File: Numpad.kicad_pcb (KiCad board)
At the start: 2 copper layers, 76.2 x 97.6 mm, 51 parts, among them J1 USB_B_Mini, SW0 0, SW1 1, SW2 2, SW3 3, SW4 4, SW5 5, SW6 6, SW7 7, SW8 8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

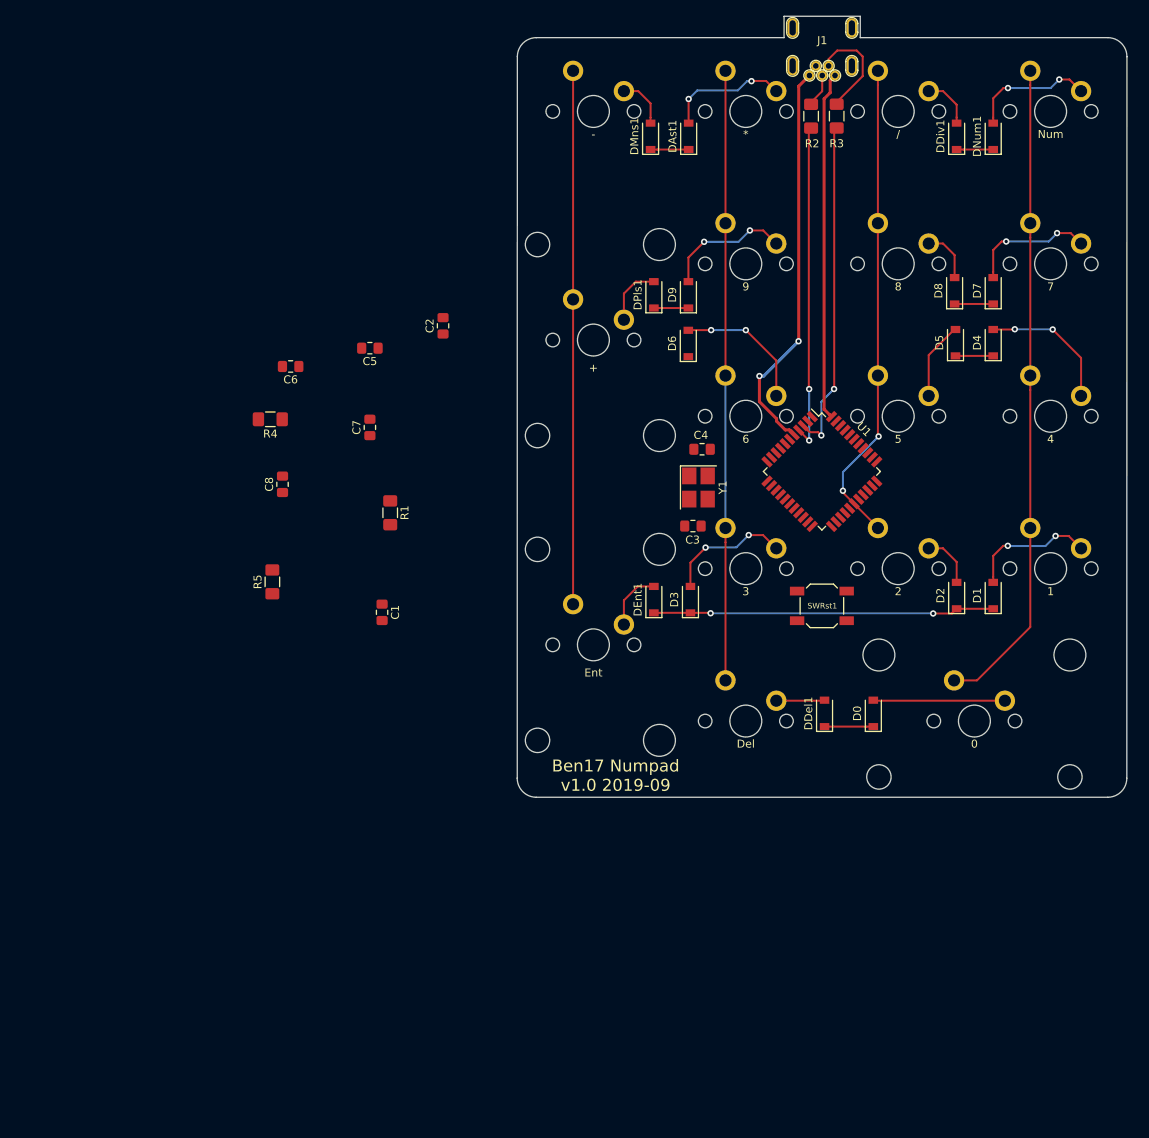
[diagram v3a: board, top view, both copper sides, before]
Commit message: allowed split + key
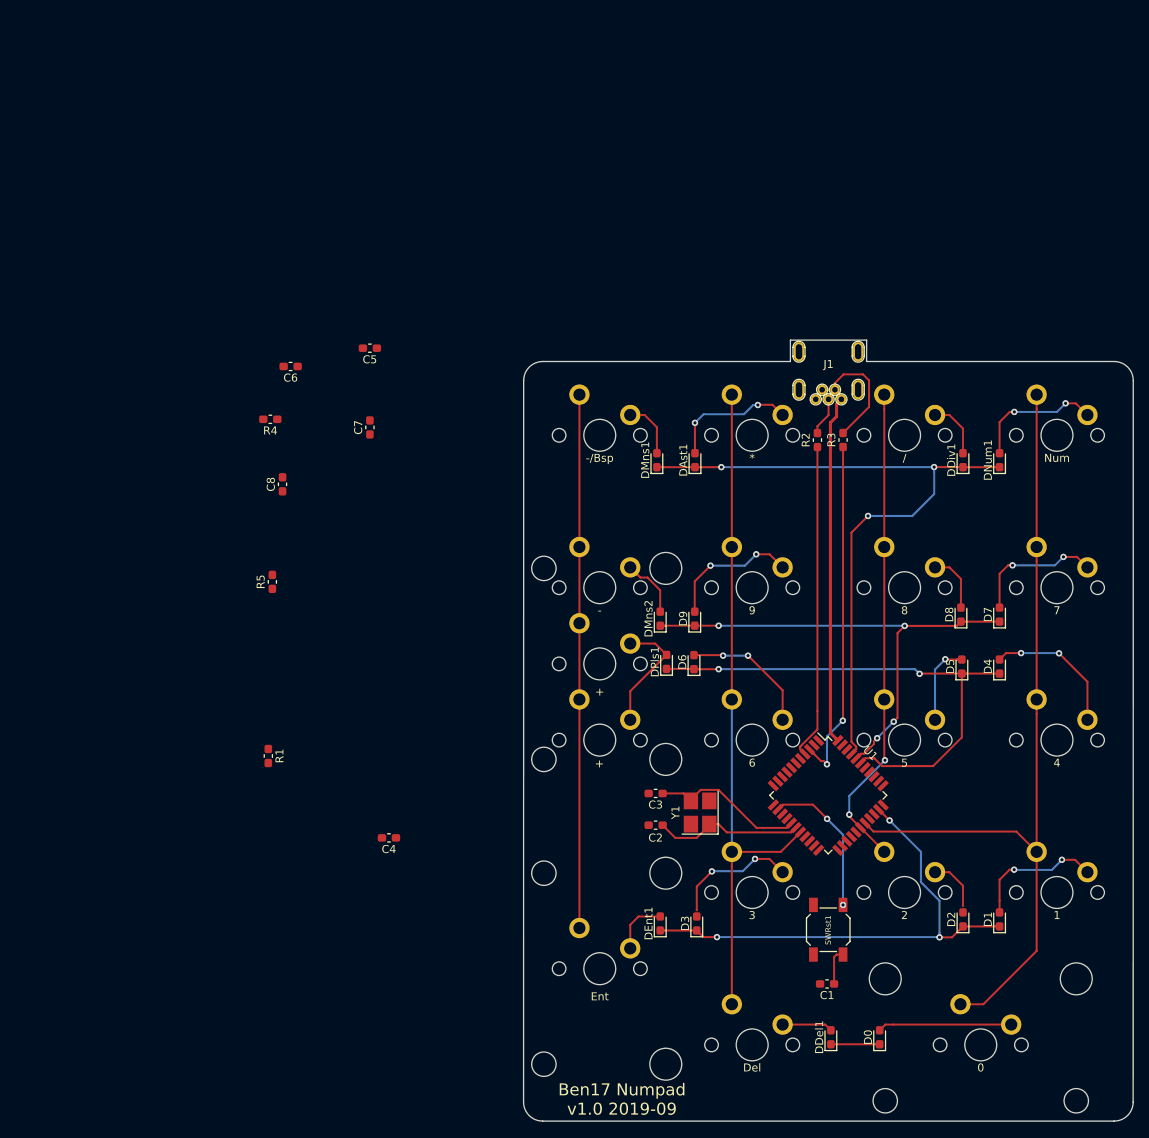
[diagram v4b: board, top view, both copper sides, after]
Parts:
- added DPls1: 1N4148W, Diode_SMD:D_0603_1608Metric_Pad1.05x0.95mm_HandSolder, F.Cu at (176.8, 117.7)
- added SWMns2: -, AcheronMX:MX100, F.Cu at (168.4, 108.4)
- added SWPls2: +, AcheronMX:MX100, F.Cu at (168.4, 127.5)
- C1: value 22pF -> 100nF; footprint Capacitor_SMD:C_0805_2012Metric_Pad1.15x1.40mm_HandSolder -> Capacitor_SMD:C_0603_1608Metric_Pad1.05x0.95mm_HandSolder
- C2, C3, C4, C5, C6, C7, C8: footprint Capacitor_SMD:C_0805_2012Metric_Pad1.15x1.40mm_HandSolder -> Capacitor_SMD:C_0603_1608Metric_Pad1.05x0.95mm_HandSolder
- D0, D1, D2, D3, D4, D5, D6, D7, D8, D9, DAst1, DDel1, DDiv1, DEnt1, DMns1, DNum1: footprint Diode_SMD:D_SOD-123 -> Diode_SMD:D_0603_1608Metric_Pad1.05x0.95mm_HandSolder
- DMns2: renamed from DPls1; footprint Diode_SMD:D_SOD-123 -> Diode_SMD:D_0603_1608Metric_Pad1.05x0.95mm_HandSolder
- R1, R2, R3, R4, R5: footprint Resistor_SMD:R_1206_3216Metric_Pad1.42x1.75mm_HandSolder -> Resistor_SMD:R_0603_1608Metric_Pad1.05x0.95mm_HandSolder
- SWMns1: value - -> -/Bsp
- moved C1 72.5 mm to (196.8, 158.0), turned to 180 degrees
- moved C2 67.8 mm to (175.4, 138.1), turned to 0 degrees
- moved C4 62.4 mm to (142.1, 139.7)
- moved Y1 40.6 mm to (181.0, 136.5), turned to 90 degrees
- moved D3 40.5 mm to (180.6, 150.4)
- moved DEnt1 40.5 mm to (176.0, 150.4)
- moved SWEnt1 40.5 mm to (168.4, 156.1)
- moved R3 40.5 mm to (198.8, 90.0)
- moved D0 40.5 mm to (203.4, 164.6)
- moved D1 40.5 mm to (218.4, 149.9)
- moved D2 40.5 mm to (213.8, 149.9)
- moved D4 40.5 mm to (218.4, 118.3)
- moved D5 40.5 mm to (213.7, 118.3)
- moved D9 40.5 mm to (180.3, 112.3)
- moved DAst1 40.5 mm to (180.3, 92.5)
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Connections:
- C1 pad 2: Net-(C1-Pad2) -> GND
- DMns2 pad 2: Net-(DPls1-Pad2) -> Net-(DMns2-Pad2)
- R5 pad 1: Net-(C1-Pad2) -> Net-(R5-Pad1)
- SWRst1 pad 2: Net-(C1-Pad2) -> Net-(R5-Pad1)
- U1 pad 18: Net-(U1-Pad18) -> Col3
- U1 pad 26: Col3 -> Net-(U1-Pad26)
- U1 pad 32: Net-(U1-Pad32) -> Row4
- U1 pad 38: Row4 -> Net-(U1-Pad38)
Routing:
- net Row1: track 9.33 -> 86.7 mm, vias 0 -> 3
- net Row3: track 4.78 -> 64.8 mm, vias 0 -> 2
- net Row2: track 9.14 -> 62.0 mm, vias 0 -> 4
- net GND: track 49.9 -> 0.00 mm, vias 2 -> 0
- net RST: track 0.00 -> 23.3 mm, vias 0 -> 2
- net Col1: track 81.8 -> 104.8 mm
- net Row4: track 42.7 -> 62.5 mm, vias 2 -> 3
- net Net-(C3-Pad1): track 0.00 -> 19.4 mm
- net Net-(C2-Pad2): track 0.00 -> 18.8 mm
- net Col3: track 76.2 -> 85.8 mm
- net Net-(DMns2-Pad2): track 0.00 -> 7.61 mm
- net Net-(DPls1-Pad2): track 7.63 -> 15.1 mm
- net D-: track 41.8 -> 43.4 mm
- net D+: track 40.9 -> 39.5 mm, vias 2 -> 0
- net Net-(D5-Pad2): track 9.78 -> 10.8 mm, vias 0 -> 1
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
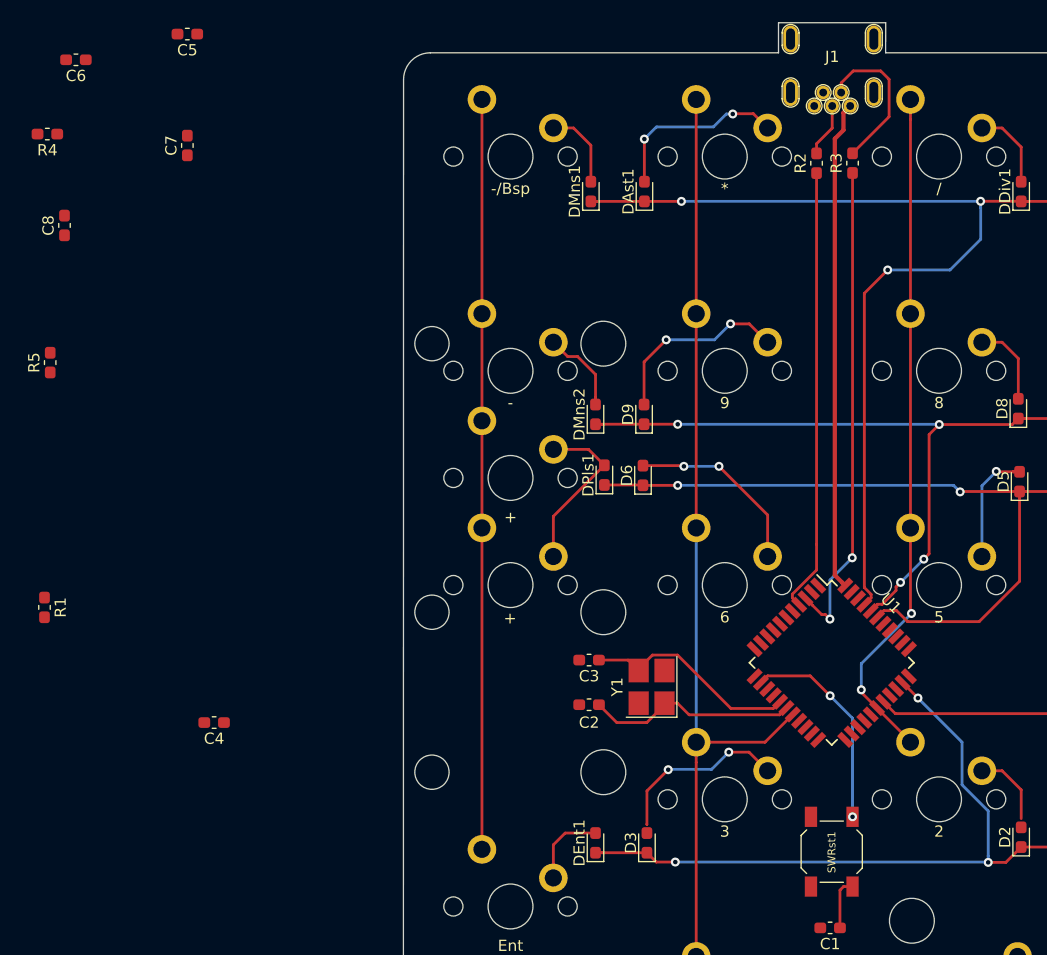
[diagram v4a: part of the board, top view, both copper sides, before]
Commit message: all componentes withing the confines of the board now, still need to add ground. Not shure about the components around reset button or c5 & c9's grounding
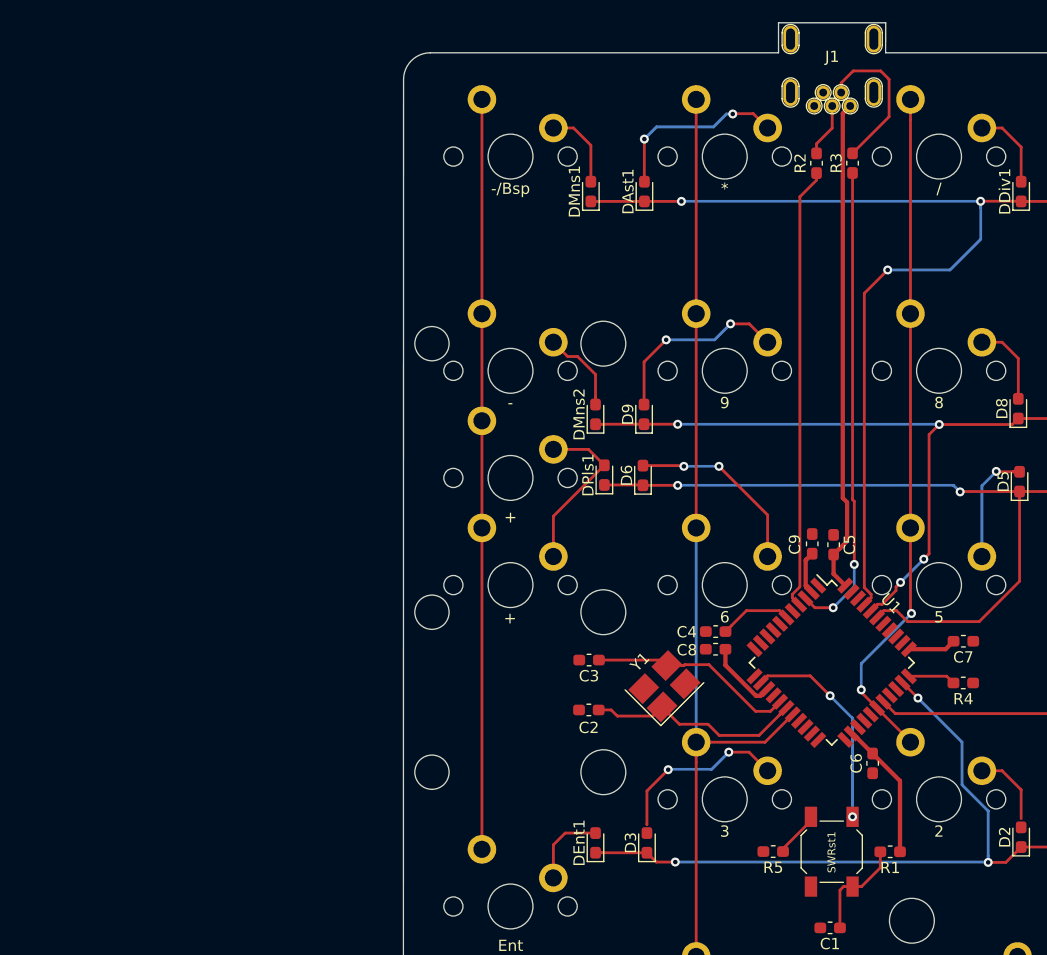
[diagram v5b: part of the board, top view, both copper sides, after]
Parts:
- added C9: 0.1uF, Capacitor_SMD:C_0603_1608Metric_Pad1.05x0.95mm_HandSolder, F.Cu at (195.3, 123.8)
- C5: value 10uF -> 4.7uF
- C6: value 1uF -> 0.1uF
- C8: value 01.uF -> 0.1uF
- moved R4 94.9 mm to (208.7, 136.2)
- moved C6 94.5 mm to (200.6, 143.3), turned to 90 degrees
- moved C7 81.9 mm to (208.7, 132.5), turned to 180 degrees
- moved R1 78.3 mm to (202.2, 151.2), turned to 180 degrees
- moved R5 77.6 mm to (191.8, 151.2), turned to 180 degrees
- moved C5 73.2 mm to (197.2, 123.9), turned to 270 degrees
- moved C8 69.1 mm to (186.7, 133.2), turned to 0 degrees
- moved C4 45.3 mm to (186.7, 131.6)
- moved Y1 1.15 mm to (182.1, 136.5), turned to 45 degrees
- moved C2 0.47 mm to (175.4, 138.6)
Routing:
- net +5V: track 43.6 -> 71.1 mm
- net Net-(C4-Pad1): track 0.00 -> 6.43 mm
- net RST: track 23.3 -> 27.9 mm
- net Net-(R4-Pad2): track 0.00 -> 4.21 mm
- net Net-(R5-Pad1): track 0.00 -> 4.12 mm
- net Net-(C2-Pad2): track 18.8 -> 20.2 mm
- net D-: track 43.4 -> 42.3 mm
- net Net-(C3-Pad1): track 19.4 -> 18.4 mm

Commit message: we can now have a maxiumum of 18 keys, so renamed it Ben18 from Ben17
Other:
- board text added: "Ben18 Numpad v1.0 2019-10"
- board text removed: "Ben17 Numpad v1.0 2019-09"
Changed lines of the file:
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@@
   (gr_line (start 201.79375 77.48125) (end 201.78625 80.15125) (layer Edge.Cuts) (width 0.05))
   (gr_line (start 192.26125 80.15125) (end 192.26125 77.48125) (layer Edge.Cuts) (width 0.05))
-  (gr_text "Ben17 Numpad\nv1.0 2019-09" (at 171.21505 172.39615) (layer F.SilkS)
+  (gr_text "Ben18 Numpad\nv1.0 2019-10" (at 171.21505 172.39615) (layer F.SilkS)
     (effects (font (size 1.5 1.5) (thickness 0.3)))
   )

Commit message: ground planes in, thinking about ordering
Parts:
- D0, D1, D2, D3, D4, D5, D6, D7, D8, D9, DAst1, DDel1, DDiv1, DEnt1, DMns1, DMns2, DNum1, DPls1: footprint Diode_SMD:D_0603_1608Metric_Pad1.05x0.95mm_HandSolder -> Diode_SMD:D_SOD-323_HandSoldering
- J1: footprint AcheronConnectors:USB_MiniB_XM7D-0512 -> digikey-kicad-library:USB_Mini_B_Female_548190519
- moved C9 56.9 mm to (146.0, 95.3)
- moved C4 56.5 mm to (137.6, 103.7)
- moved C8 56.5 mm to (137.6, 105.3)
- moved C5 56.4 mm to (148.4, 95.4)
- moved R3 56.4 mm to (148.1, 65.4)
- moved D6 56.2 mm to (131.4, 90.0)
- moved C1 56.2 mm to (148.0, 130.2)
- moved C2 56.2 mm to (126.6, 110.8)
- moved C6 56.2 mm to (151.8, 115.6)
- moved D3 56.2 mm to (131.7, 122.7)
- moved DEnt1 56.2 mm to (127.2, 122.7)
- moved SWEnt1 56.2 mm to (119.6, 128.3)
- moved D1 56.2 mm to (169.6, 122.2)
- moved D2 56.2 mm to (165.0, 122.2)
- moved D4 56.2 mm to (169.6, 90.6)
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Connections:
- R2 pad 1: D+ -> D-
- R2 pad 2: Net-(J1-Pad3) -> Net-(J1-Pad2)
- R3 pad 1: D- -> D+
- R3 pad 2: Net-(J1-Pad2) -> Net-(J1-Pad3)
- U1 pad 19: Net-(U1-Pad19) -> Col4
- U1 pad 25: Col4 -> Net-(U1-Pad25)
- U1 pad 26: Net-(U1-Pad26) -> Row5
- U1 pad 37: Row5 -> Net-(U1-Pad37)
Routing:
- net Col4: track 66.7 -> 99.6 mm, vias 0 -> 1
- net GND: track 0.00 -> 31.1 mm, vias 0 -> 4
- net +5V: track 71.1 -> 99.3 mm
- net Row5: track 6.10 -> 33.6 mm
- net Net-(J1-Pad2): track 13.8 -> 5.80 mm
- net RST: track 27.9 -> 35.6 mm
- net Net-(R5-Pad1): track 4.12 -> 8.25 mm
- net Net-(DDel1-Pad2): track 6.33 -> 8.12 mm
- net Net-(J1-Pad3): track 4.79 -> 3.12 mm
- net Net-(D3-Pad2): track 15.8 -> 14.5 mm
- net Net-(DEnt1-Pad2): track 7.12 -> 5.99 mm
- net D-: track 42.3 -> 41.4 mm
- net Net-(D0-Pad2): track 16.7 -> 17.6 mm
- net Row2: track 62.0 -> 61.2 mm
- net Net-(D1-Pad2): track 16.8 -> 16.1 mm
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- added copper zone on B.Cu, net GND
- added copper zone on F.Cu, net GND
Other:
- board size 76.2 x 97.6 mm -> 76.2 x 95 mm

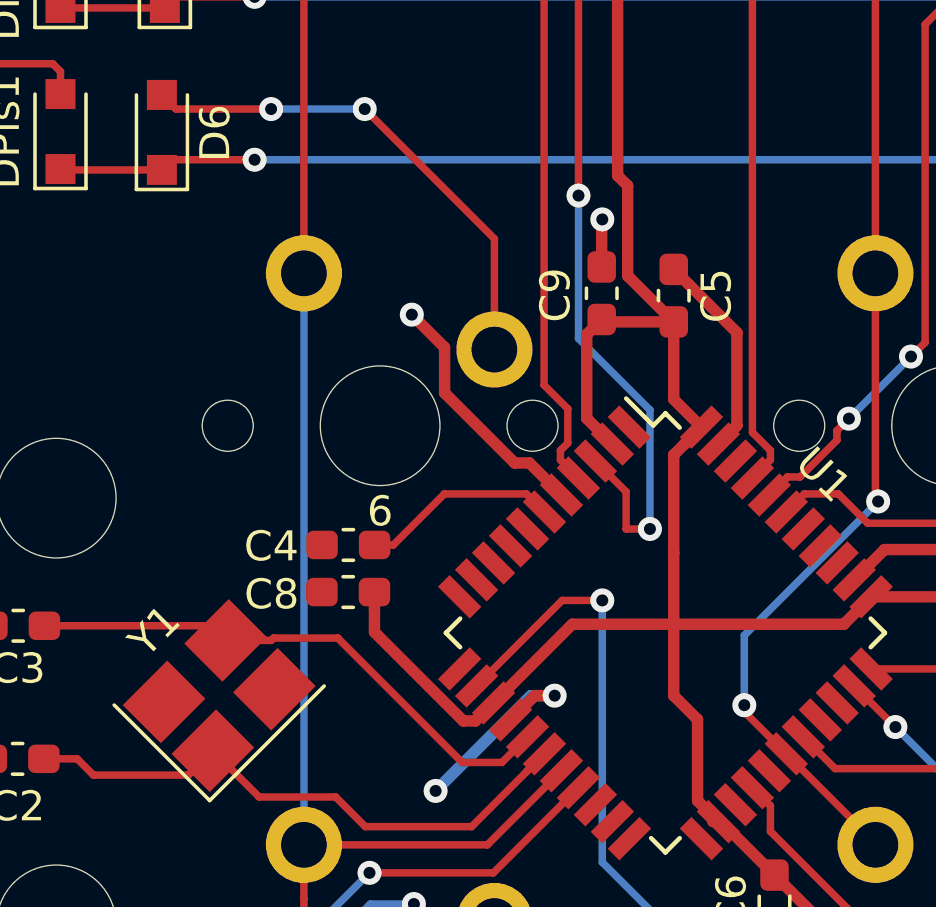
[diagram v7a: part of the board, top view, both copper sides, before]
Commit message: two of the capacitors needed larger footprints, have added BoM
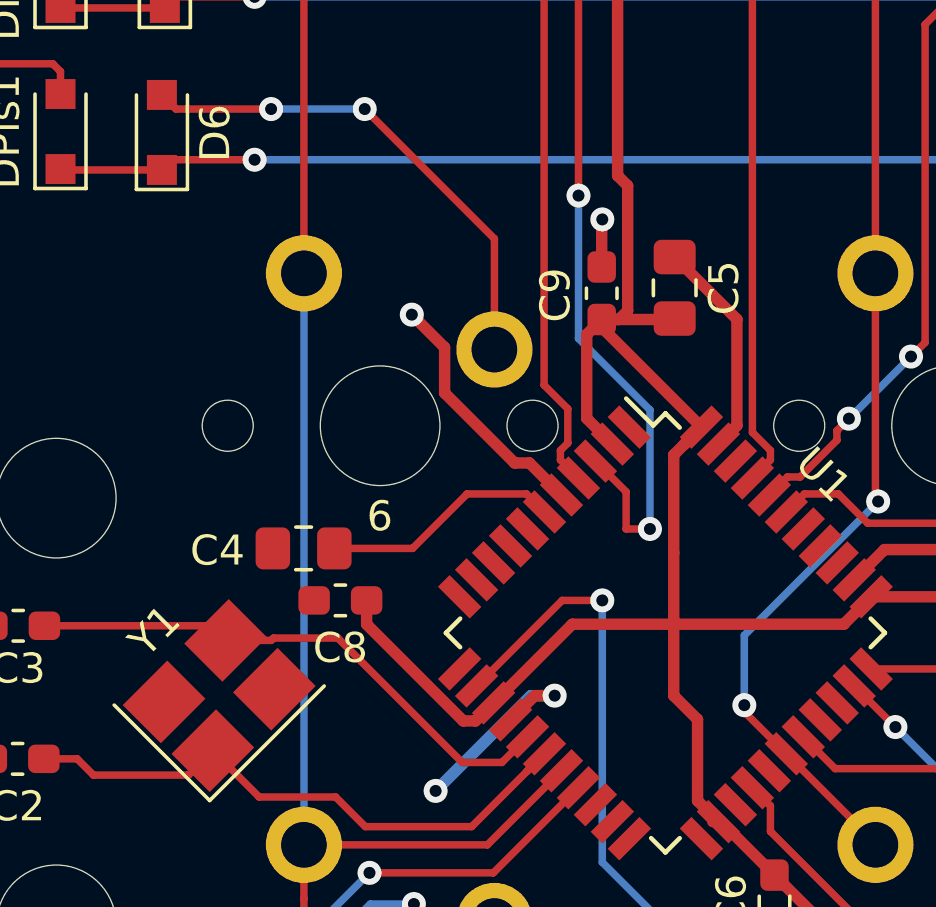
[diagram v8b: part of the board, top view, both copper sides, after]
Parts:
- C1: value 100nF -> 0.1uF
- C4, C5: footprint Capacitor_SMD:C_0603_1608Metric_Pad1.05x0.95mm_HandSolder -> Capacitor_SMD:C_0805_2012Metric_Pad1.15x1.40mm_HandSolder
- moved C4 1.50 mm to (136.1, 103.8)
- moved C8 0.38 mm to (137.3, 105.6)
- moved C5 0.26 mm to (148.5, 95.1)
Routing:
- net Net-(C4-Pad1): track 6.62 -> 8.01 mm
- net +5V: track 99.3 -> 100.4 mm
